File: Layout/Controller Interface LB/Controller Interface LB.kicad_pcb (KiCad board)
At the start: 2 copper layers, 50 x 50 mm, 19 parts, among them J1 Conn_01x08_Socket

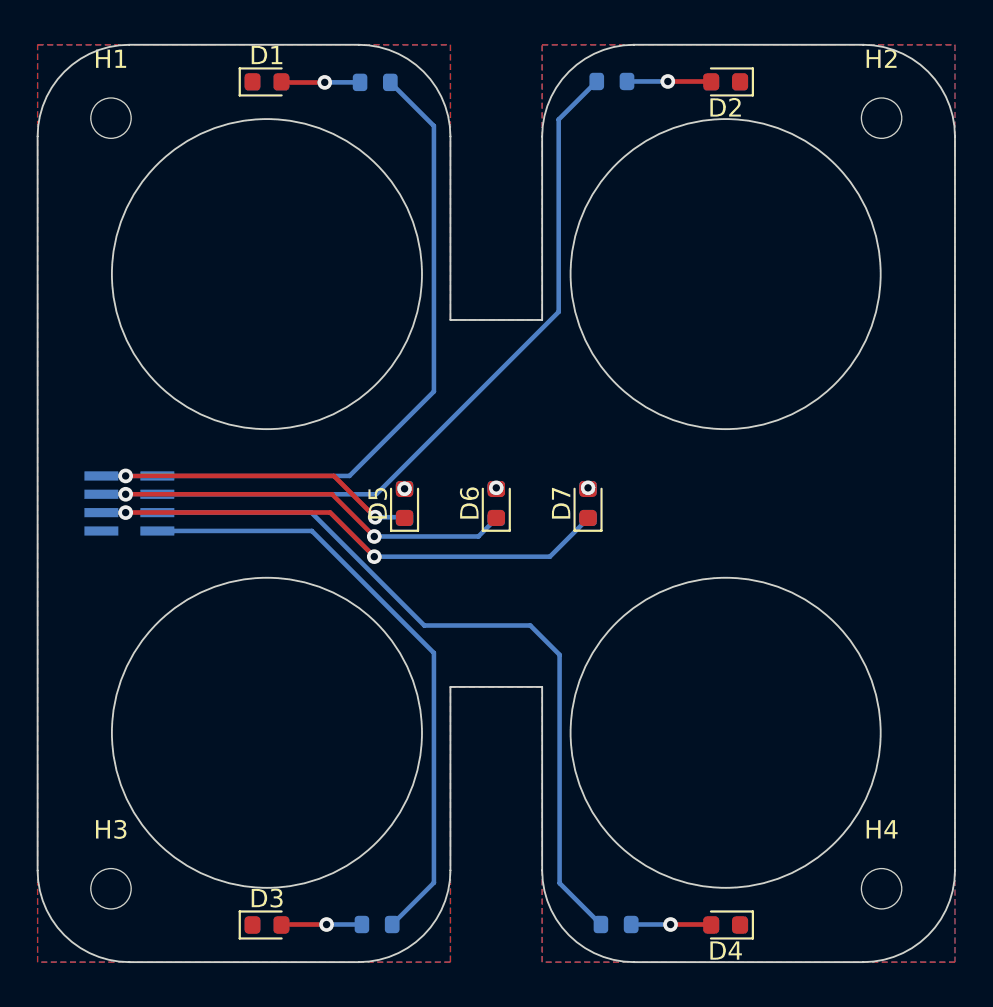
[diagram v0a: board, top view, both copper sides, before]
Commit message: Use separate board for lights
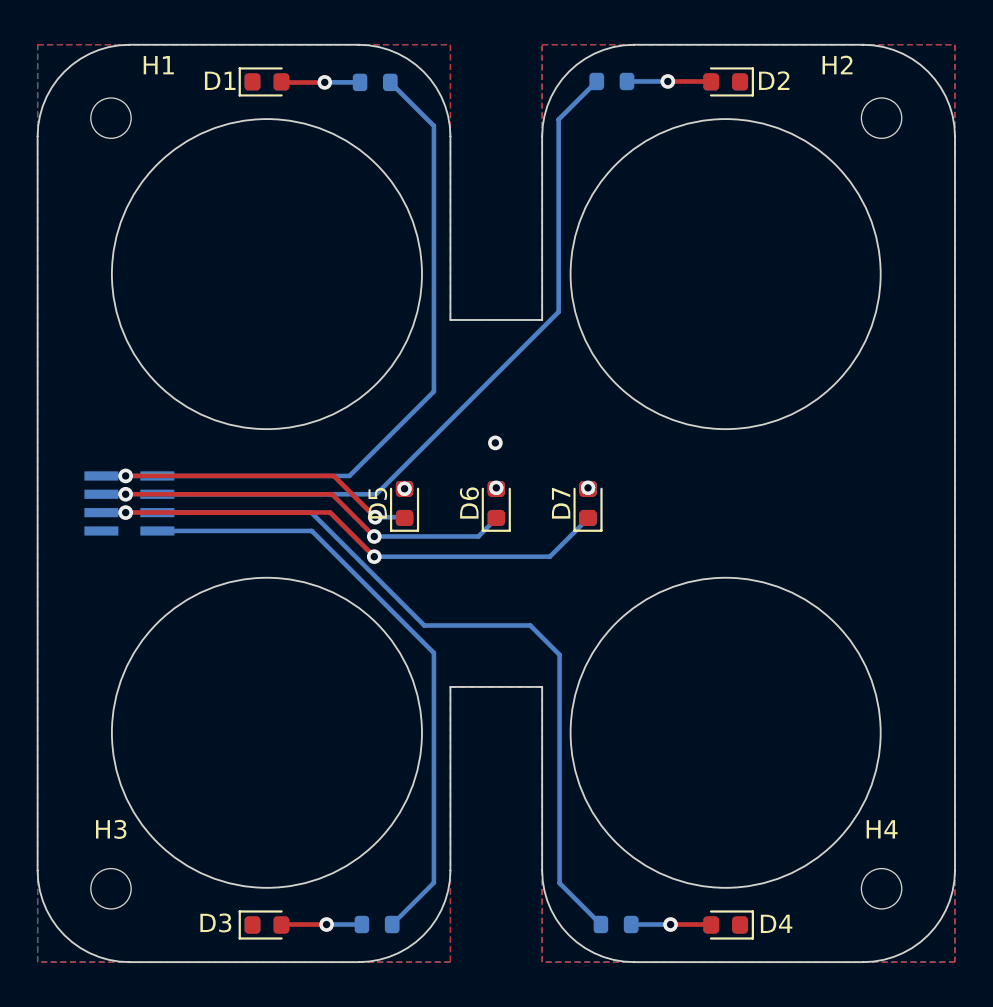
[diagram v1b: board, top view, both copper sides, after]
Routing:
- net GND: vias 0 -> 1
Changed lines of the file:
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@@
       (plot_on_all_layers_selection 0x0000000_00000000)
       (disableapertmacros false)
-      (usegerberextensions false)
-      (usegerberattributes true)
-      (usegerberadvancedattributes true)
-      (creategerberjobfile true)
+      (usegerberextensions true)
+      (usegerberattributes false)
+      (usegerberadvancedattributes false)
+      (creategerberjobfile false)
       (dashed_line_dash_ratio 12.000000)
       (dashed_line_gap_ratio 3.000000)
@@
       (psa4output false)
       (plotreference true)
-      (plotvalue true)
+      (plotvalue false)
       (plotinvisibletext false)
       (sketchpadsonfab false)
-      (subtractmaskfromsilk false)
+      (subtractmaskfromsilk true)
       (outputformat 1)
       (mirror false)
-      (drillshape 1)
+      (drillshape 0)
       (scaleselection 1)
-      (outputdirectory "")
+      (outputdirectory "Output/")
     )
   )
@@
     (property "ki_keywords" "LED diode")
     (attr smd)
-    (fp_text reference "D1" (at 0 -1.43) (layer "F.SilkS")
+    (fp_text reference "D1" (at -2.55 -0.025) (layer "F.SilkS")
         (effects (font (size 1 1) (thickness 0.15)))
     )
@@
     (property "ki_keywords" "mounting hole")
     (attr exclude_from_pos_files)
-    (fp_text reference "H2" (at 0 -3.2) (layer "F.SilkS")
+    (fp_text reference "H2" (at -2.4 -2.85) (layer "F.SilkS")
         (effects (font (size 1 1) (thickness 0.15)))
     )
@@
     (property "ki_keywords" "mounting hole")
     (attr exclude_from_pos_files)
-    (fp_text reference "H1" (at 0 -3.2) (layer "F.SilkS")
+    (fp_text reference "H1" (at 2.6 -2.85) (layer "F.SilkS")
         (effects (font (size 1 1) (thickness 0.15)))
     )
@@
     (property "ki_keywords" "LED diode")
     (attr smd)
-    (fp_text reference "D4" (at 0 -1.43) (layer "F.SilkS")
+    (fp_text reference "D4" (at -2.75 0.025) (layer "F.SilkS")
         (effects (font (size 1 1) (thickness 0.15)))
     )
@@
     (property "ki_keywords" "LED diode")
     (attr smd)
-    (fp_text reference "D2" (at 0 -1.43) (layer "F.SilkS")
+    (fp_text reference "D2" (at -2.65 0.025) (layer "F.SilkS")
         (effects (font (size 1 1) (thickness 0.15)))
     )
@@
     (property "ki_keywords" "LED diode")
     (attr smd)
-    (fp_text reference "D3" (at 0 -1.43) (layer "F.SilkS")
+    (fp_text reference "D3" (at -2.8 -0.075) (layer "F.SilkS")
         (effects (font (size 1 1) (thickness 0.15)))
     )
@@
         (effects (font (size 1 1) (thickness 0.15)) (justify mirror))
     )
-    (fp_text user "${REFERENCE}" (at 0 0 90) (layer "B.Fab")
+    (fp_text user "${REFERENCE}" (at 2.4 3.5) (layer "B.Fab")
         (effects (font (size 1 1) (thickness 0.15)) (justify mirror))
     )
@@
     (property "ki_keywords" "R res resistor")
     (attr smd)
-    (fp_text reference "R1" (at 0 1.43) (layer "B.SilkS")
+    (fp_text reference "R1" (at 0.05 -1.4) (layer "B.SilkS")
         (effects (font (size 1 1) (thickness 0.15)) (justify mirror))
     )
@@
     (property "ki_keywords" "R res resistor")
     (attr smd)
-    (fp_text reference "R4" (at 0 1.43) (layer "B.SilkS")
+    (fp_text reference "R4" (at 0 -1.45) (layer "B.SilkS")
         (effects (font (size 1 1) (thickness 0.15)) (justify mirror))
     )
@@
   (gr_arc (start 163.8 58.6) (mid 167.335534 60.064466) (end 168.8 63.6)
     (stroke (width 0.1) (type default)) (layer "Edge.Cuts"))
+  (via (at 143.75 80.3) (size 0.8) (drill 0.4) (layers "F.Cu" "B.Cu") (free) (net 1))
   (segment (start 134.45 60.65) (end 132.1125 60.65) (width 0.25) (layer "F.Cu") (net 2))
   (segment (start 132.1125 60.65) (end 132.0875 60.625) (width 0.25) (layer "F.Cu") (net 2))
@@
     (connect_pads (clearance 0))
     (min_thickness 0.25) (filled_areas_thickness no)
-    (fill (thermal_gap 0.5) (thermal_bridge_width 0.5))
+    (fill yes (thermal_gap 0.5) (thermal_bridge_width 0.5))
     (polygon
       (pts
